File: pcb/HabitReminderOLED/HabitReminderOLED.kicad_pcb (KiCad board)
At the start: 2 copper layers, 64.8 x 53.3 mm, 33 parts, among them J1 I2C Sockets, J2 UART Pins, J3 USB_C_Receptacle_USB2.0_16P, Q2 S8050, Q3 S8050, SW1 PUSH_1, SW2 PUSH_2, SW3 PUSH_3, U1 ESP32-WROOM-32D, U2 CP2102N-Axx-xQFN28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

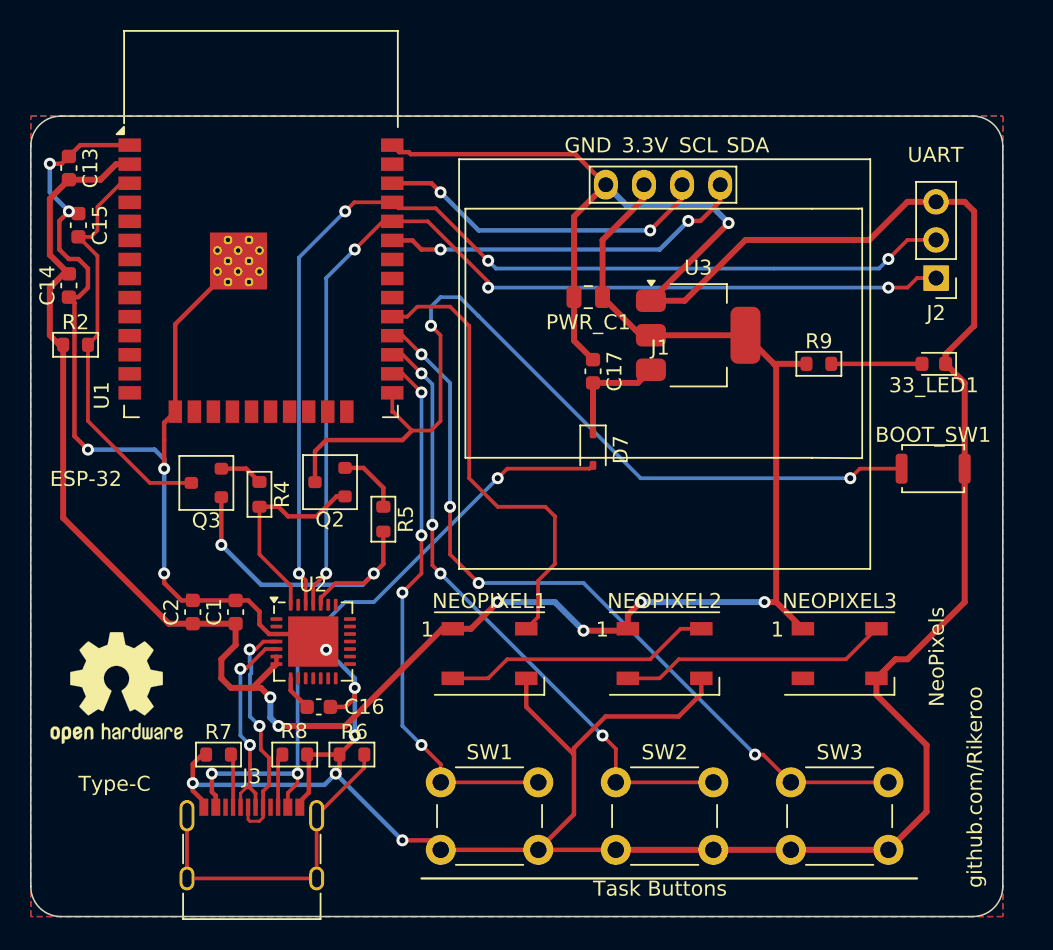
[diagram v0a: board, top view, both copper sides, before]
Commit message: Move to SMD buttons, added LCSC designators
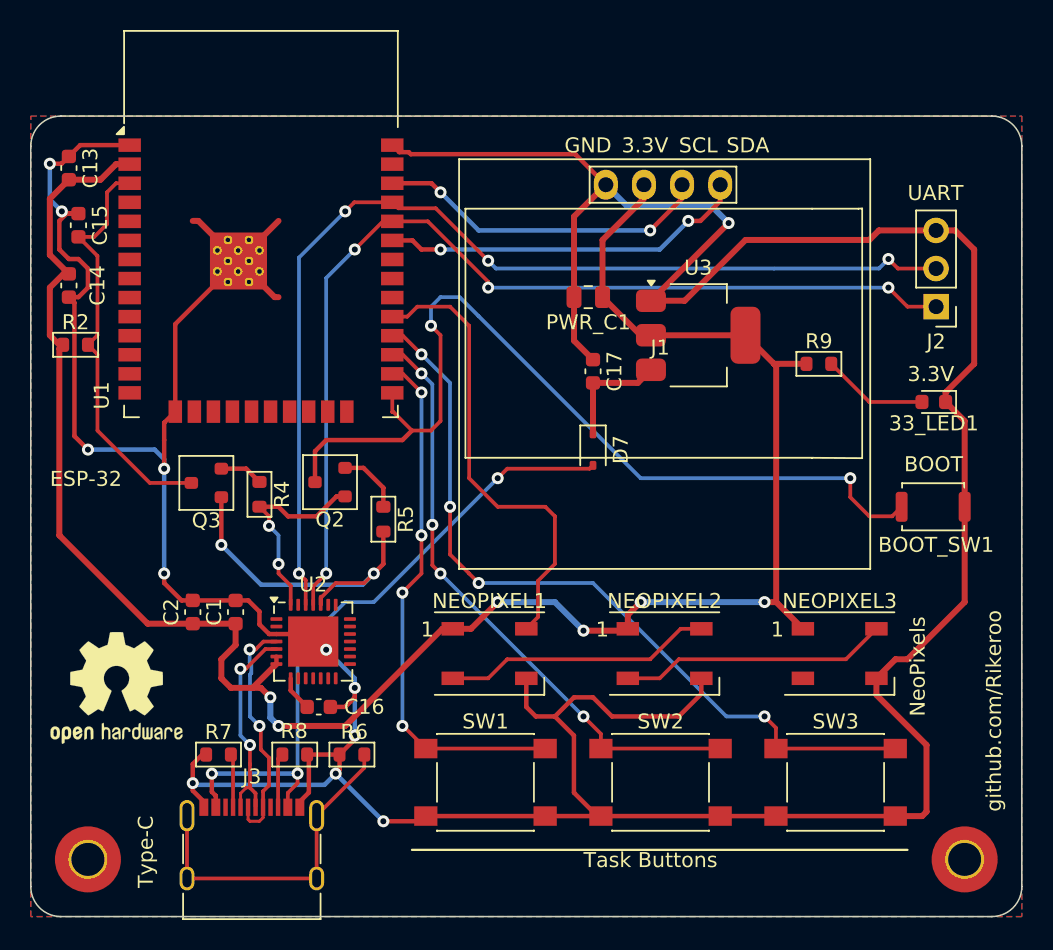
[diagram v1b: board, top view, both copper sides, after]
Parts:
- added REF**: MountingHole_2.2mm_M2_Pad_TopOnly, MountingHole:MountingHole_2.2mm_M2_Pad_TopOnly, F.Cu at (148.6, 118.7)
- added REF**: MountingHole_2.2mm_M2_Pad_TopOnly, MountingHole:MountingHole_2.2mm_M2_Pad_TopOnly, F.Cu at (90.2, 118.7)
- SW1, SW2, SW3: footprint Button_Switch_THT:SW_PUSH_6mm -> Button_Switch_SMD:SW_Push_1P1T_NO_6x6mm_H9.5mm
- moved SW3 2.98 mm to (140.0, 113.6)
- moved SW1 2.98 mm to (116.7, 113.6)
- moved SW2 2.98 mm to (128.3, 113.6)
- moved 33_LED1 2.54 mm to (146.5, 88.3)
- moved BOOT_SW1 2.54 mm to (146.5, 95.2)
- moved J2 1.91 mm to (146.7, 81.9)
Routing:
- net GND: track 284.5 -> 286.6 mm
- net /BOOT: track 59.1 -> 60.9 mm
- net /PUSH_2: track 41.6 -> 40.4 mm
- net /PUSH_1: track 36.5 -> 35.3 mm
- net Net-(33_LED1-A): track 6.05 -> 7.10 mm
- net +3.3V: track 137.6 -> 138.7 mm
- net /EN: track 27.5 -> 28.4 mm
- net /DTR: vias 0 -> 2
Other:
- board size 64.8 x 53.3 mm -> 66 x 53.3 mm
- board text added: "BOOT"
